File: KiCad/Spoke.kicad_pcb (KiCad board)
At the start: 2 copper layers, 50 x 100 mm, 131 parts, among them J1 B2B-PH-K-S, J10 BL-A, J11 BL-C, J12 Amphenol 132289, J2 BAT+, J3 BAT-, J4 GCT USB4105/USB4110, J5 CHG+, J6 CHG-, J7 PLS-1x3, J8 PLS-1x6, J9 PLS-1x3, Q1 AO3407A, Q2 AO3400, Q3 AO3400, Q4 AO3400, SW1 PWR, SW2 OK/UP, SW3 ESC/DN, SW4 BOOT, U1 SP0503BAHTG, U2 TP4056, U3 CP2102N-A02-GQFN28, U4 LM3671MF-3.3, U5 74HC4052PW, U6 STM32F103C8T6, U7 LSM303DLHC, X1 8MHz

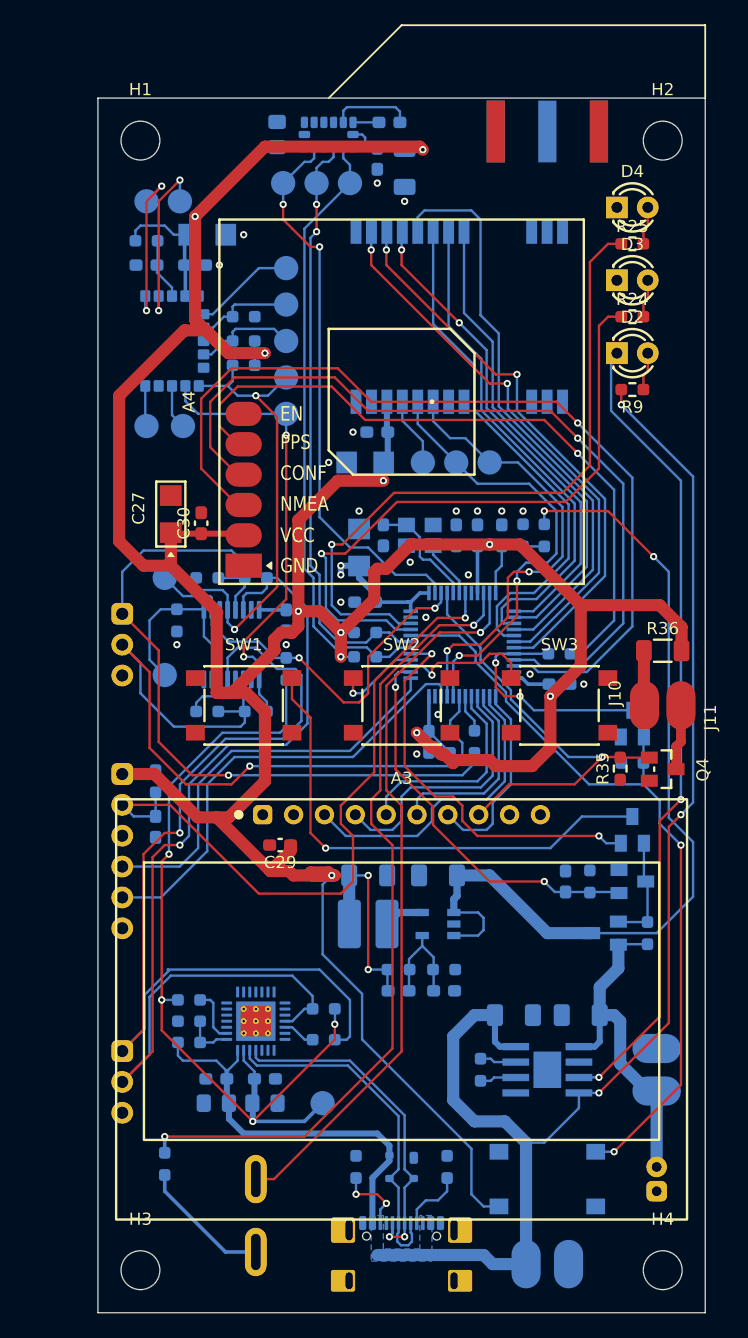
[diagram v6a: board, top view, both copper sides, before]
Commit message: Update SCH with notes, add R23
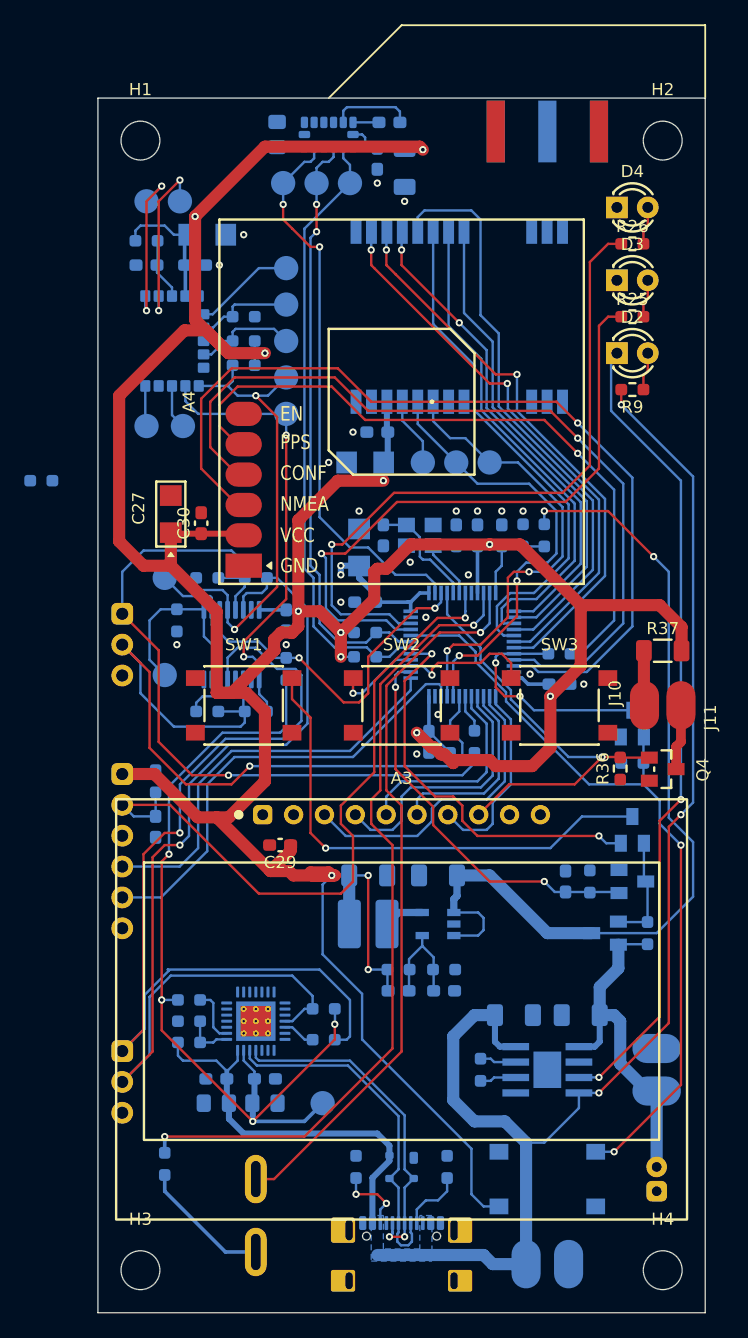
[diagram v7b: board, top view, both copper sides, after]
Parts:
- added R23: 0R, Spoke:R0603, B.Cu at (70.3, 81.5)
- J5: value CHG+ -> USB+
- J6: value CHG- -> USB-
- renumbered R23 to R24, R24 to R25, R25 to R26, R26 to R28, R28 to R29, R29 to R30, R30 to R31, R31 to R32, R32 to R33, R33 to R34, R34 to R35, R35 to R36, R36 to R37, R37 to R38, R38 to R39
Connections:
- net Net-(A1-WAKEUP/SLEEP) renamed BLE_WKP_SLP
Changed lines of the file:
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@@
 	(net 56 "GPS_TXD")
 	(net 57 "Net-(A1-SWDCLK)")
-	(net 58 "Net-(A1-WAKEUP{slash}SLEEP)")
+	(net 58 "BLE_WKP_SLP")
 	(net 59 "unconnected-(A1-NC-Pad10)")
 	(net 60 "Net-(A1-DISC)")
@@
 		(layer "F.Cu")
 		(at 121.5 95.5)
-		(property "Reference" "R36"
+		(property "Reference" "R37"
 			(at 0 -1.83 0)
 			(layer "F.SilkS")
@@
 		(layer "F.Cu")
 		(at 118 105.2 90)
-		(property "Reference" "R35"
+		(property "Reference" "R36"
 			(at 0 -1.43 90)
 			(layer "F.SilkS")
@@
 		(layer "F.Cu")
 		(at 119 62)
-		(property "Reference" "R25"
+		(property "Reference" "R26"
 			(at 0 -1.43 0)
 			(layer "F.SilkS")
@@
 		(layer "F.Cu")
 		(at 119 68)
-		(property "Reference" "R24"
+		(property "Reference" "R25"
 			(at 0 -1.43 0)
 			(layer "F.SilkS")
@@
 		(layer "B.Cu")
 		(at 87 76 180)
-		(property "Reference" "R23"
+		(property "Reference" "R24"
 			(at 0 1.43 0)
 			(layer "B.SilkS")
@@
 		(layer "B.Cu")
 		(at 84 89.5 180)
-		(property "Reference" "R31"
+		(property "Reference" "R32"
 			(at 0 1.43 0)
 			(layer "B.SilkS")
@@
 		(layer "B.Cu")
 		(at 111.75 86 90)
-		(property "Reference" "R33"
+		(property "Reference" "R34"
 			(at 0 1.43 90)
 			(layer "B.SilkS")
@@
 			(size 2 2)
 			(layers "B.Cu" "B.Mask" "B.Paste")
-			(net 58 "Net-(A1-WAKEUP{slash}SLEEP)")
+			(net 58 "BLE_WKP_SLP")
 			(pinfunction "1")
 			(pintype "unspecified")
@@
 		(layer "B.Cu")
 		(at 87 72 180)
-		(property "Reference" "R26"
+		(property "Reference" "R28"
 			(at 0 1.43 0)
 			(layer "B.SilkS")
@@
 			)
 		)
-		(property "Value" "CHG+"
+		(property "Value" "USB+"
 			(at -0.01092 -2.58572 90)
 			(layer "B.Fab")
@@
 		(layer "B.Cu")
 		(at 97 96 180)
-		(property "Reference" "R37"
+		(property "Reference" "R38"
 			(at 0 1.43 0)
 			(layer "B.SilkS")
@@
 		(layer "B.Cu")
 		(at 88 100.5)
-		(property "Reference" "R32"
+		(property "Reference" "R33"
 			(at 0 1.43 0)
 			(layer "B.SilkS")
@@
 			)
 		)
-		(property "Value" "CHG-"
+		(property "Value" "USB-"
 			(at -0.01092 -2.58572 90)
 			(layer "B.Fab")
@@
 		(layer "B.Cu")
 		(at 79 61.75)
-		(property "Reference" "R30"
+		(property "Reference" "R31"
 			(at 0 1.43 0)
 			(layer "B.SilkS")
@@
 		(layer "B.Cu")
 		(at 87 68)
-		(property "Reference" "R28"
+		(property "Reference" "R29"
 			(at 0 1.43 180)
 			(layer "B.SilkS")
@@
 			(layers "B.Cu" "B.Mask" "B.Paste")
 			(roundrect_rratio 0.25)
-			(net 58 "Net-(A1-WAKEUP{slash}SLEEP)")
+			(net 58 "BLE_WKP_SLP")
 			(pinfunction "1")
 			(pintype "unspecified")
@@
 		(embedded_fonts no)
 	)
+	(footprint "Spoke:R0603"
+		(layer "B.Cu")
+		(at 70.3375 81.5 180)
+		(property "Reference" "R23"
+			(at 0 1.43 0)
+			(layer "B.SilkS")
+			(effects
+				(font
+					(size 1 1)
+					(thickness 0.15)
+				)
+				(justify mirror)
+			)
+		)
+		(property "Value" "0R"
+			(at 0 -1.43 0)
+			(layer "B.Fab")
+			(effects
+				(font
+					(size 1 1)
+					(thickness 0.15)
+				)
+				(justify mirror)
+			)
+		)
+		(property "Datasheet" ""
+			(at 0 0 0)
+			(layer "B.Fab")
+			(hide yes)
+			(effects
+				(font
+					(size 1.27 1.27)
+					(thickness 0.15)
+				)
+				(justify mirror)
+			)
+		)
+		(property "Description" ""
+			(at 0 0 0)
+			(layer "B.Fab")
+			(hide yes)
+			(effects
+				(font
+					(size 1.27 1.27)
+					(thickness 0.15)
+				)
+				(justify mirror)
+			)
+		)
+		(sheetname "/")
+		(sheetfile "Spoke.kicad_sch")
+		(attr smd dnp)
+		(fp_line
+			(start -0.254724 0.5225)
+			(end 0.254724 0.5225)
+			(stroke
+				(width 0.2)
+				(type solid)
+			)
+			(layer "B.SilkS")
+		)
+		(fp_line
+			(start -0.254724 -0.5225)
+			(end 0.254724 -0.5225)
+			(stroke
+				(width 0.2)
+				(type solid)
+			)
+			(layer "B.SilkS")
+		)
+		(fp_rect
+			(start -1.6 0.7)
+			(end 1.6 -0.7)
+			(stroke
+				(width 0.2)
+				(type default)
+			)
+			(fill no)
+			(layer "B.CrtYd")
+		)
+		(pad "1" smd roundrect
+			(at -0.9125 0 180)
+			(size 0.975 0.95)
+			(layers "B.Cu" "B.Mask" "B.Paste")
+			(roundrect_rratio 0.25)
+			(net 58 "BLE_WKP_SLP")
+			(pinfunction "1")
+			(pintype "unspecified")
+		)
+		(pad "2" smd roundrect
+			(at 0.9125 0 180)
+			(size 0.975 0.95)
+			(layers "B.Cu" "B.Mask" "B.Paste")
+			(roundrect_rratio 0.25)
+			(net 49 "MUX_BLE_USB")
+			(pinfunction "2")
+			(pintype "unspecified")
+		)
+		(embedded_fonts no)
+		(model "${KIPRJMOD}/packages3d/R_0603_1608Metric.step"
+			(offset
+				(xyz 0 0 0)
+			)
+			(scale
+				(xyz 1 1 1)
+			)
+			(rotate
+				(xyz 0 0 0)
+			)
+		)
+	)
 	(footprint "Spoke:Pad_round"
 		(layer "B.Cu")
@@
 			(layers "B.Cu" "B.Mask" "B.Paste")
 			(roundrect_rratio 0.15)
-			(net 58 "Net-(A1-WAKEUP{slash}SLEEP)")
+			(net 58 "BLE_WKP_SLP")
 			(pinfunction "WAKEUP/SLEEP")
 			(pintype "unspecified")
@@
 		(layer "B.Cu")
 		(at 110 86 -90)
-		(property "Reference" "R34"
+		(property "Reference" "R35"
 			(at 0 1.43 90)
 			(layer "B.SilkS")
@@
 		(layer "B.Cu")
 		(at 97 94 180)
-		(property "Reference" "R38"
+		(property "Reference" "R39"
 			(at 0 1.43 0)
 			(layer "B.SilkS")
@@
 		(layer "B.Cu")
 		(at 87 70 180)
-		(property "Reference" "R29"
+		(property "Reference" "R30"
 			(at 0 1.43 0)
 			(layer "B.SilkS")

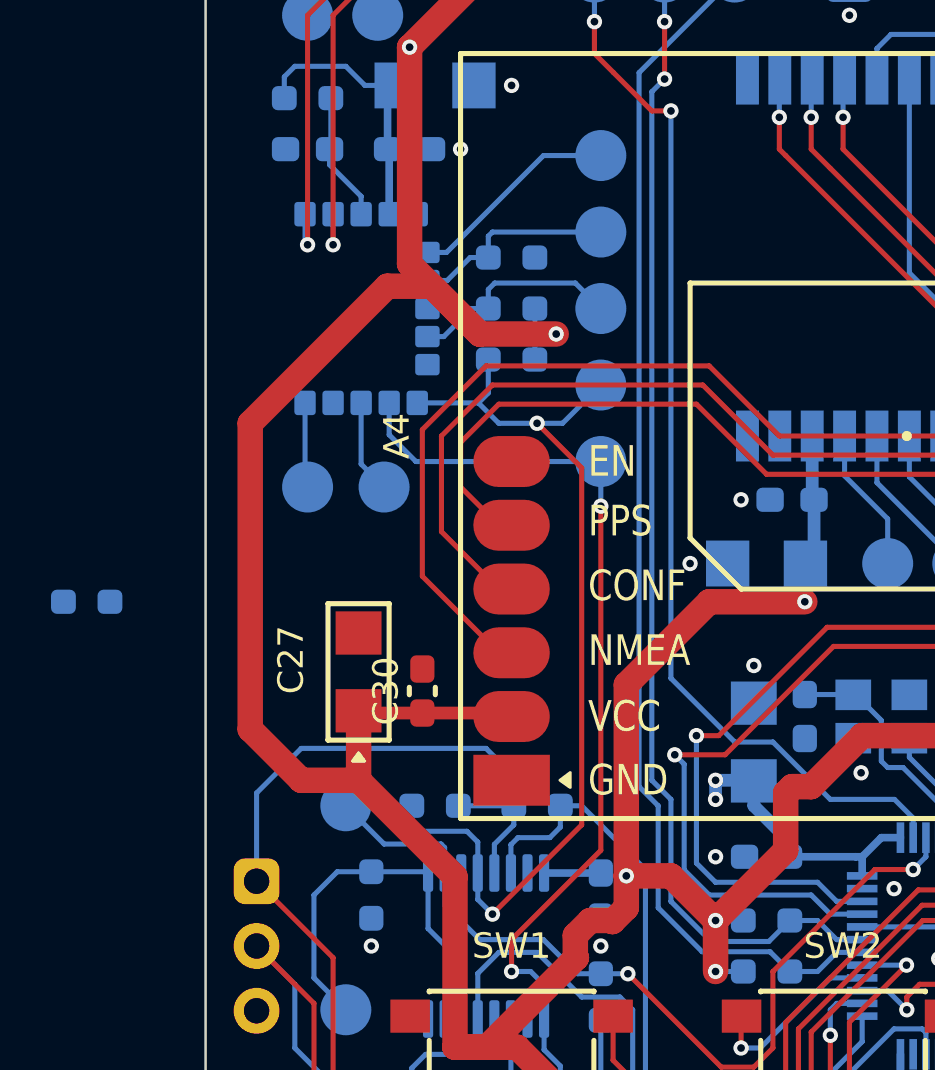
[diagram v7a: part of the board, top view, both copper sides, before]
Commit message: Route R23
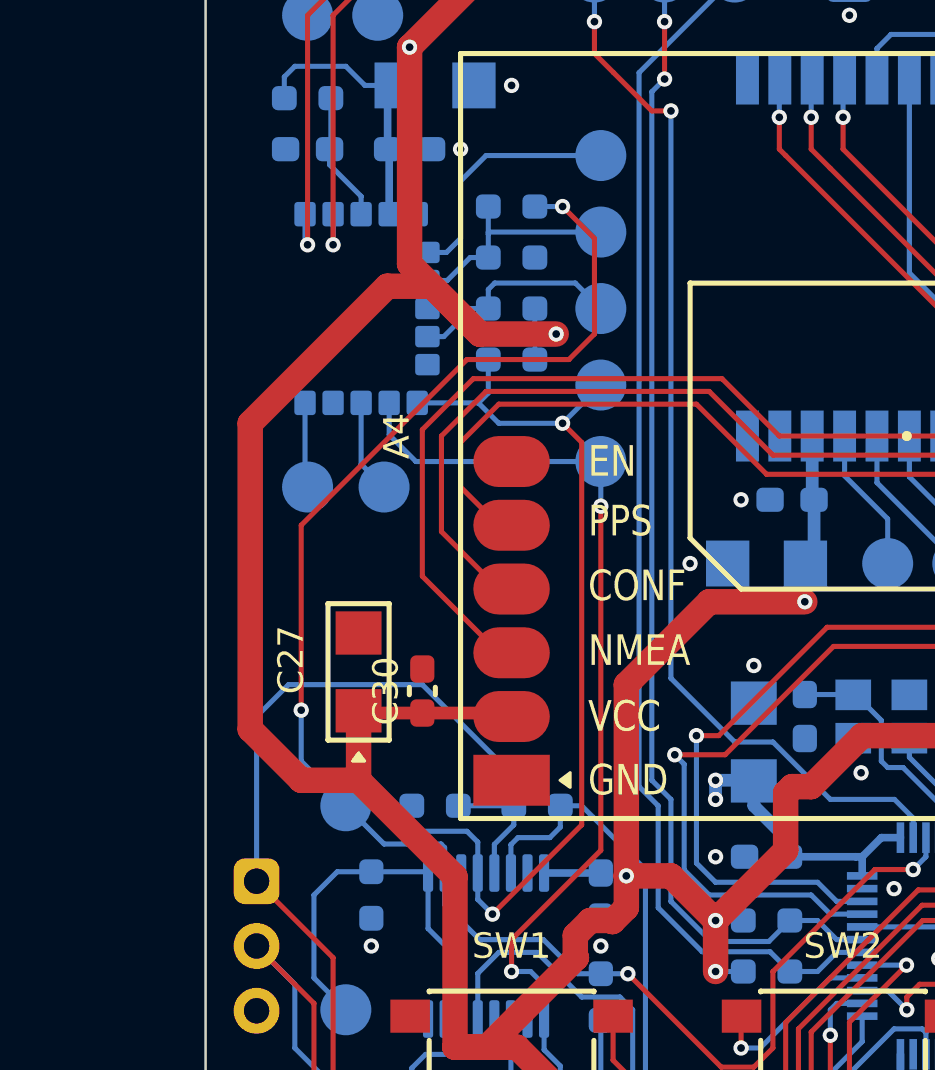
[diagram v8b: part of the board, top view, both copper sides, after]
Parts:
- moved R23 22.8 mm to (87.0, 66.0), turned to 0 degrees
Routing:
- net MUX_BLE_USB: track 34.2 -> 67.2 mm, vias 2 -> 4
- net CONSOLE_TXD: track 61.2 -> 65.0 mm
- net Net-(A1-DISC): track 8.37 -> 9.69 mm
- net BLE_WKP_SLP: track 8.08 -> 9.26 mm
